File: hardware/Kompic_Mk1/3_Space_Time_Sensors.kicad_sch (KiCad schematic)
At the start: 38 parts, among them CN1 Qvar_Electrode_2, U5 LSM6DSV16XTR, U6 MAX-M10S-00B, U7 LIS3MDLTR, U8 PCF85063ATL/1,118, X1 FC31M2-32.768-NTLLLDT

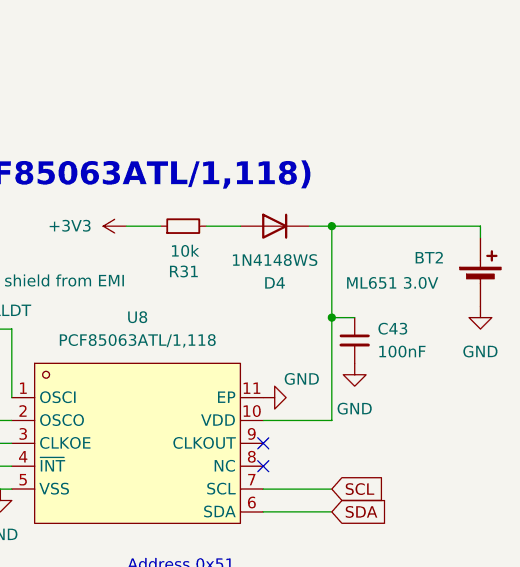
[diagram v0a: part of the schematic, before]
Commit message: Added Circuit page! Minor touchups to schematic + Schematic PDF.
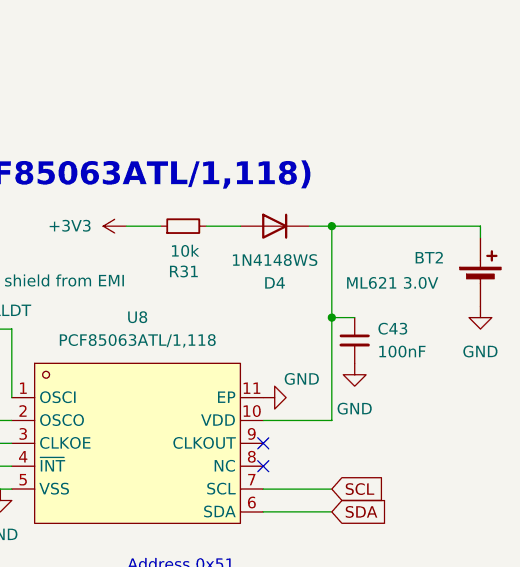
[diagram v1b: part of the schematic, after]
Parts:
- BT2: value ML651 3.0V -> ML621 3.0V
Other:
- company: Ivan Porupski May2026(c) -> Ivan Porupski June2026(c)
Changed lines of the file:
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@@
 	(paper "A4")
 	(title_block
-		(date "2026-05-30")
-		(rev "iv7.0")
-		(company "Ivan Porupski May2026(c)")
+		(date "2026-06-02")
+		(rev "iv7.1")
+		(company "Ivan Porupski June2026(c)")
 	)
 	(text "SDO/SA0: Tie to VDD_IO (1.8V) → address 0x6B.\nMandatory, BQ25619 owns 0x6A."
@@
 			)
 		)
-		(property "Value" "ML651 3.0V"
+		(property "Value" "ML621 3.0V"
 			(at 261.874 120.65 0)
 			(show_name no)

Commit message: MASSIVE UPDATE: Built a working prototype with most systems go! iv7.1 requires about half a dozen surgical hacks on the PCB itself - it is suggested you wait for iv7.2+ - but otherwise, a massive success!
Stage 1-3 documents how the parts were added, in what fashion and then tested both electrically and with the scripts in test/ for each stage. SD Card may be unfixable in iv7.1.

Added notes where the bugs are in the schematic, but haven't updated it.
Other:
- note added: "BUG: VDD AND VDD_IO SWAPPED ON LSM AND LIS"
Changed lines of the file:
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@@
+		)
+	)
+	(text "BUG: VDD AND VDD_IO SWAPPED ON LSM AND LIS"
+		(exclude_from_sim no)
+		(at 131.318 31.75 0)
+		(effects
+			(font
+				(size 2.54 2.54)
+				(thickness 0.508)
+				(bold yes)
+				(color 255 38 26 1)
+			)
 		)
 	)
